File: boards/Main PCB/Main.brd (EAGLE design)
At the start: 101.6 x 76.2 mm, 89 parts, among them CN1 MINIB, CN2 MINIB, IC1 FT232RL, IC2 FT232RL, J1 3_PIN_JST-XH, J2 2_PIN_JST-XH, Q4 BSS138, Q5 BSS138, Q6 BSS138, Q7 BSS138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

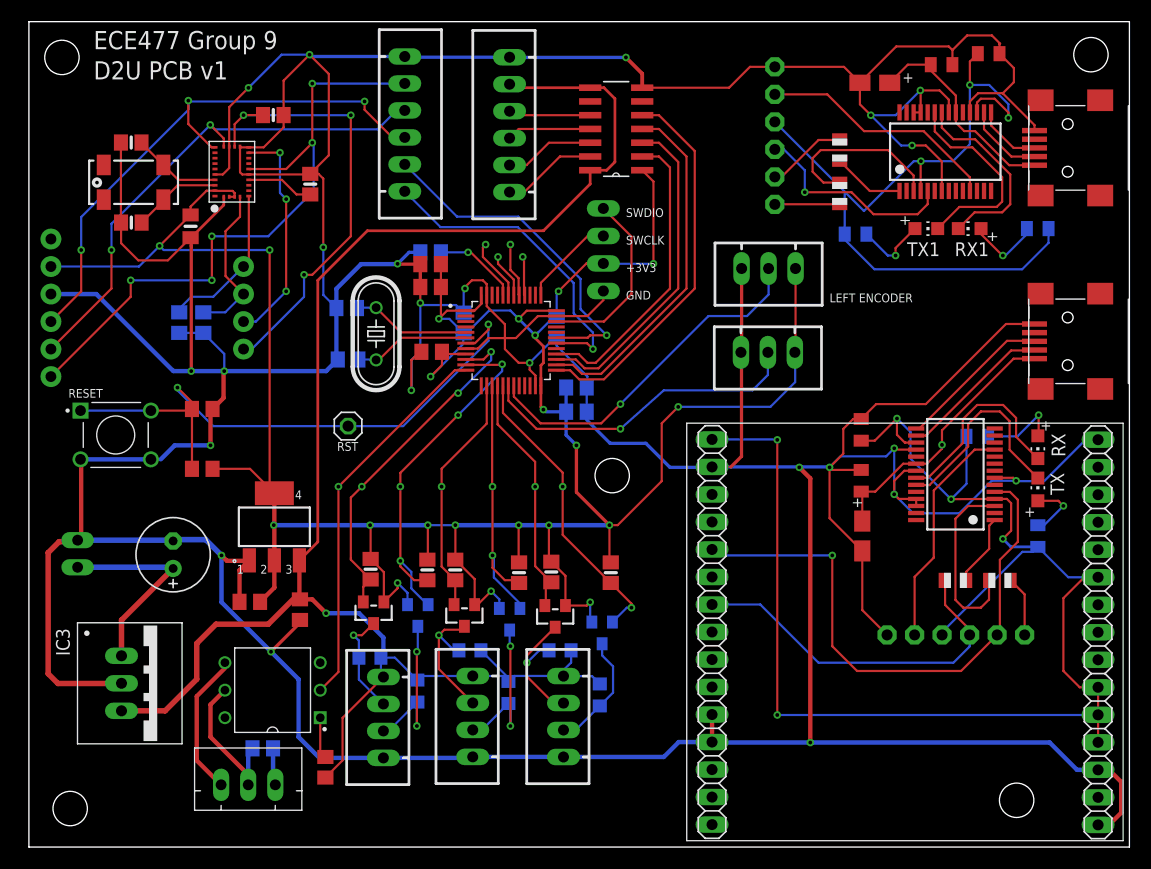
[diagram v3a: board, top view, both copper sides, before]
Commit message: More improvements on trace widths, orientations
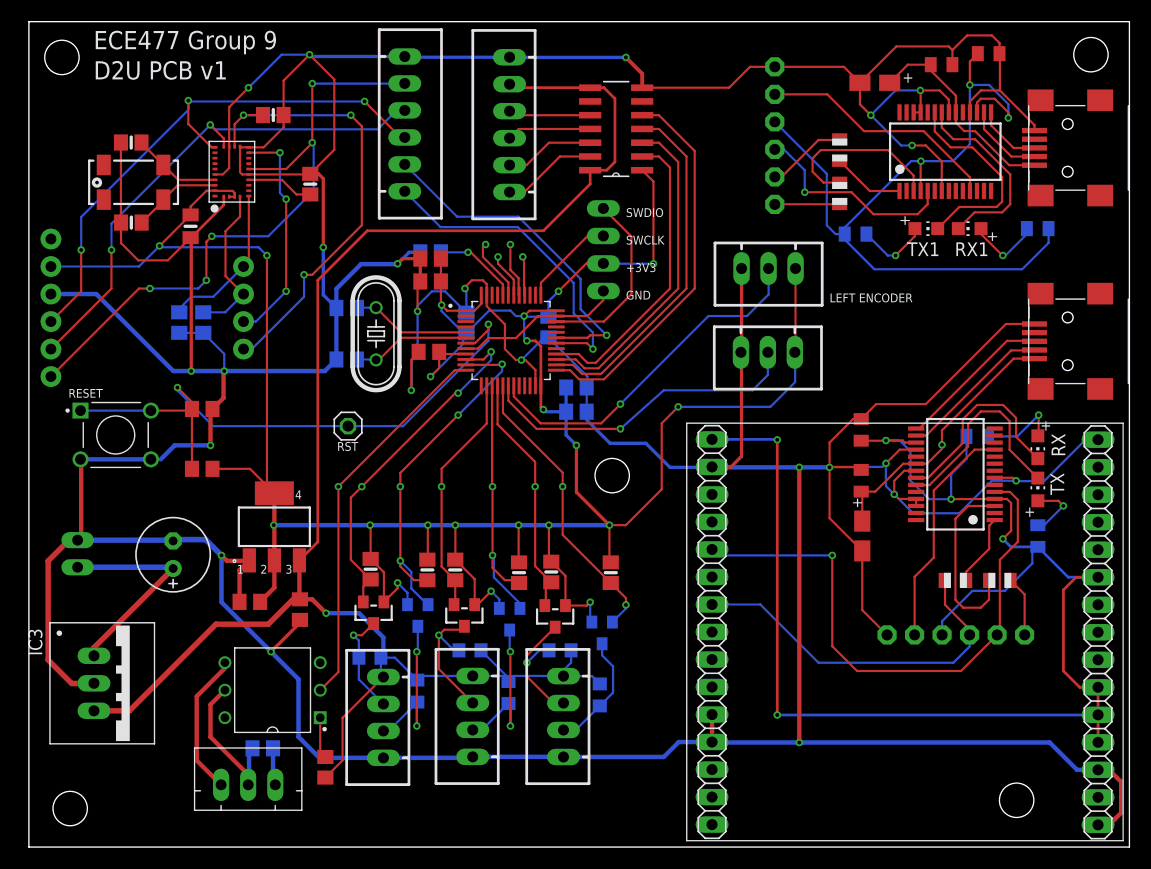
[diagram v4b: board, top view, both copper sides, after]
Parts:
- moved IC3 2.54 mm to (7.28, 15.1)
- moved C24 0.76 mm to (48.0, 48.0)
- moved C20 0.51 mm to (37.1, 54.3)
- moved C25 0.51 mm to (37.1, 52.2)
- moved C22 0.25 mm to (36.9, 45.7)
- moved C21 0.25 mm to (40.4, 48.4)
- moved C15 0.13 mm to (29.3, 45.0)
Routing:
- net GND: track 672.1 -> 668.6 mm
- net NRESET_3V: track 60.0 -> 58.8 mm
- net 12V_IN: track 18.9 -> 20.0 mm
- net +3V3_LIDAR: track 72.6 -> 73.6 mm
- net I2CADDR_3V: track 41.5 -> 42.4 mm
- net US3_ECHO: track 27.7 -> 27.0 mm
- net +3V3_UART_GPS: track 136.3 -> 135.6 mm
- net +5V: track 154.9 -> 155.5 mm

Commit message: More minor trace improvements
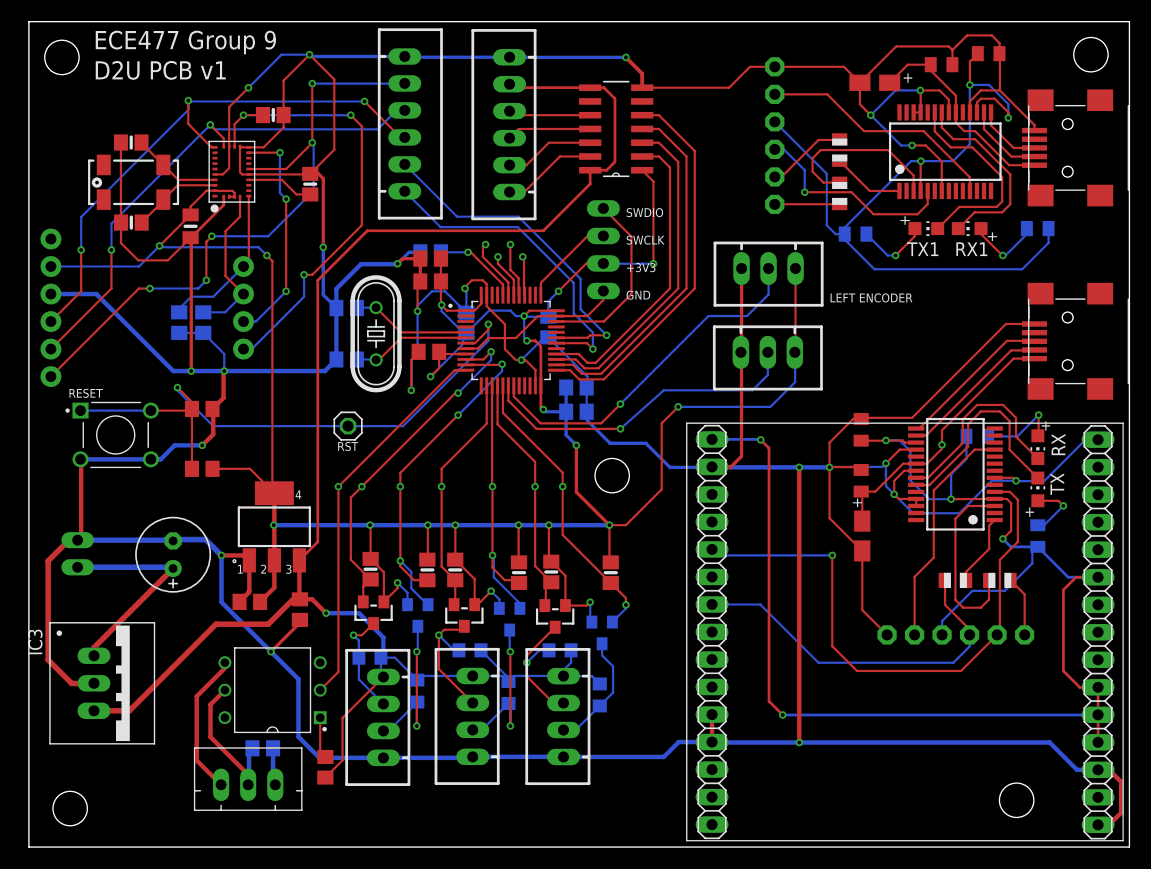
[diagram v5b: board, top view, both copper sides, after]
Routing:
- net +3V3_UART_GPS: track 135.6 -> 134.5 mm
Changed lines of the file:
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@@
 <wire x1="76.936" y1="27.341" x2="76.936" y2="21.876" width="0.2032" layer="1"/>
 <wire x1="76.936" y1="21.876" x2="79.226" y2="19.586" width="0.2032" layer="1"/>
-<wire x1="76.836" y1="39.516" x2="78.214" y2="40.894" width="0.2032" layer="1"/>
-<wire x1="78.214" y1="40.894" x2="82.804" y2="40.894" width="0.2032" layer="1"/>
-<wire x1="82.804" y1="40.894" x2="90.2" y2="48.29" width="0.2032" layer="1"/>
+<wire x1="76.836" y1="39.516" x2="76.944" y2="39.624" width="0.2032" layer="1"/>
+<wire x1="76.944" y1="39.624" x2="81.534" y2="39.624" width="0.2032" layer="1"/>
+<wire x1="81.534" y1="39.624" x2="90.2" y2="48.29" width="0.2032" layer="1"/>
 <wire x1="90.2" y1="48.29" x2="92.836" y2="48.29" width="0.2032" layer="1"/>
 <wire x1="68.862" y1="72.03" x2="75.243" y2="72.03" width="0.2032" layer="1"/>
@@
 <wire x1="4.496" y1="28.332" x2="4.826" y2="28.662" width="0.4064" layer="1"/>
 <wire x1="4.826" y1="35.732" x2="4.764" y2="35.794" width="0.2032" layer="1"/>
-<wire x1="11.264" y1="35.794" x2="12.172" y2="35.794" width="0.2032" layer="16"/>
-<wire x1="13.462" y1="37.084" x2="16.764" y2="37.084" width="0.4064" layer="16"/>
+<wire x1="11.264" y1="35.794" x2="12.172" y2="35.794" width="0.4064" layer="16"/>
+<wire x1="13.462" y1="37.084" x2="16.002" y2="37.084" width="0.4064" layer="16"/>
 <wire x1="12.172" y1="35.794" x2="13.462" y2="37.084" width="0.4064" layer="16"/>
-<via x="16.764" y="37.084" extent="1-16" drill="0.35"/>
-<wire x1="16.764" y1="37.084" x2="16.764" y2="40.256" width="0.4064" layer="1"/>
-<wire x1="16.764" y1="40.256" x2="16.952" y2="40.444" width="0.2032" layer="1"/>
+<via x="16.002" y="37.084" extent="1-16" drill="0.35"/>
+<wire x1="17.018" y1="40.378" x2="17.018" y2="38.1" width="0.4064" layer="1"/>
+<wire x1="16.002" y1="37.084" x2="17.018" y2="38.1" width="0.4064" layer="1"/>
+<wire x1="16.952" y1="40.444" x2="17.018" y2="40.378" width="0.4064" layer="1"/>
 <wire x1="16.952" y1="40.444" x2="17.968" y2="41.46" width="0.4064" layer="1"/>
 <wire x1="27.317" y1="43.942" x2="28.387" y2="45.012" width="0.4064" layer="16"/>
@@
 <wire x1="27.178" y1="50.974" x2="27.178" y2="55.372" width="0.3048" layer="16"/>
 <via x="27.178" y="55.372" extent="1-16" drill="0.35"/>
-<wire x1="19.444" y1="22.638" x2="19.444" y2="25.5646" width="0.4064" layer="1"/>
-<wire x1="19.444" y1="25.5646" x2="20.3077" y2="26.4283" width="0.4064" layer="1"/>
 <via x="34.036" y="53.848" extent="1-16" drill="0.35"/>
 <wire x1="20.3077" y1="26.4283" x2="20.3486" y2="26.4692" width="0.2032" layer="1"/>
@@
 <wire x1="40.974" y1="8.3262" x2="49.342" y2="8.3262" width="0.4064" layer="16"/>
 <wire x1="49.342" y1="8.3262" x2="49.352" y2="8.3162" width="0.2032" layer="16"/>
-<wire x1="18.2757" y1="26.4283" x2="20.3077" y2="26.4283" width="0.4064" layer="1"/>
-<wire x1="17.78" y1="26.924" x2="18.2757" y2="26.4283" width="0.4064" layer="1"/>
 <wire x1="34.698" y1="72.983" x2="26.077" y2="72.983" width="0.3048" layer="16"/>
 <wire x1="26.077" y1="72.983" x2="25.908" y2="73.152" width="0.3048" layer="16"/>
@@
 <wire x1="89.604" y1="73.246" x2="89.64" y2="73.21" width="0.2032" layer="1"/>
 <wire x1="89.64" y1="73.21" x2="89.64" y2="69.85" width="0.2032" layer="1"/>
+<wire x1="17.78" y1="26.924" x2="19.812" y2="26.924" width="0.4064" layer="1"/>
+<wire x1="19.812" y1="26.924" x2="20.3077" y2="26.4283" width="0.4064" layer="1"/>
+<wire x1="20.3486" y1="26.4692" x2="20.3486" y2="23.6173375" width="0.4064" layer="1"/>
+<wire x1="20.3486" y1="23.6173375" x2="20.2876" y2="23.5563375" width="0.4064" layer="1"/>
+<wire x1="20.2876" y1="23.5563375" x2="20.2876" y2="23.4816" width="0.4064" layer="1"/>
+<wire x1="20.2876" y1="23.4816" x2="19.444" y2="22.638" width="0.4064" layer="1"/>
 </signal>
 <signal name="D+_GPS">
@@
 <wire x1="70.739" y1="42.926" x2="70.739" y2="45.6452" width="0.2032" layer="16"/>
 <wire x1="70.739" y1="45.6452" x2="70.7112" y2="45.673" width="0.2032" layer="16"/>
-<wire x1="22.66" y1="32.667" x2="21.971" y2="33.356" width="0.2032" layer="1"/>
-<wire x1="21.971" y1="33.356" x2="21.971" y2="54.61" width="0.2032" layer="1"/>
+<wire x1="22.66" y1="32.667" x2="22.479" y2="32.848" width="0.2032" layer="1"/>
+<wire x1="22.479" y1="54.102" x2="21.971" y2="54.61" width="0.2032" layer="1"/>
+<wire x1="22.479" y1="54.102" x2="22.479" y2="32.848" width="0.2032" layer="1"/>
 <via x="21.971" y="54.61" extent="1-16" drill="0.35"/>
 <wire x1="21.971" y1="54.61" x2="21.209" y2="55.372" width="0.2032" layer="16"/>
@@
 <wire x1="98.703" y1="24.908" x2="96.671" y2="24.908" width="0.254" layer="1"/>
 <wire x1="96.671" y1="24.908" x2="95.504" y2="23.741" width="0.254" layer="1"/>
-<wire x1="63.0668" y1="37.6334" x2="69.0466" y2="37.6334" width="0.254" layer="16"/>
-<wire x1="69.0466" y1="37.6334" x2="69.088" y2="37.592" width="0.2032" layer="16"/>
-<via x="69.088" y="37.592" extent="1-16" drill="0.35"/>
-<wire x1="69.088" y1="37.592" x2="69.088" y2="12.192" width="0.254" layer="1"/>
-<via x="69.088" y="12.192" extent="1-16" drill="0.35"/>
-<wire x1="69.088" y1="12.192" x2="98.687" y2="12.192" width="0.254" layer="16"/>
+<via x="67.564" y="37.592" extent="1-16" drill="0.35"/>
+<wire x1="68.326" y1="36.83" x2="67.564" y2="37.592" width="0.254" layer="1"/>
+<wire x1="68.326" y1="36.83" x2="68.326" y2="13.462" width="0.254" layer="1"/>
+<wire x1="69.596" y1="12.192" x2="68.326" y2="13.462" width="0.254" layer="1"/>
+<via x="69.596" y="12.192" extent="1-16" drill="0.35"/>
+<wire x1="69.596" y1="12.192" x2="98.687" y2="12.192" width="0.254" layer="16"/>
 <wire x1="98.687" y1="12.192" x2="98.703" y2="12.208" width="0.2032" layer="16"/>
 <wire x1="93.144" y1="27.716" x2="95.952" y2="24.908" width="0.254" layer="16"/>
@@
 <wire x1="80.861" y1="37.341" x2="80.668" y2="37.534" width="0.2032" layer="1"/>
 <wire x1="80.668" y1="37.534" x2="79.122" y2="37.534" width="0.2032" layer="1"/>
+<wire x1="67.5226" y1="37.6334" x2="67.564" y2="37.592" width="0.254" layer="16"/>
+<wire x1="63.0668" y1="37.6334" x2="67.5226" y2="37.6334" width="0.254" layer="16"/>
 </signal>
 <signal name="US2_ECHO">

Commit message: Added pullup resistors for SDA and SCL
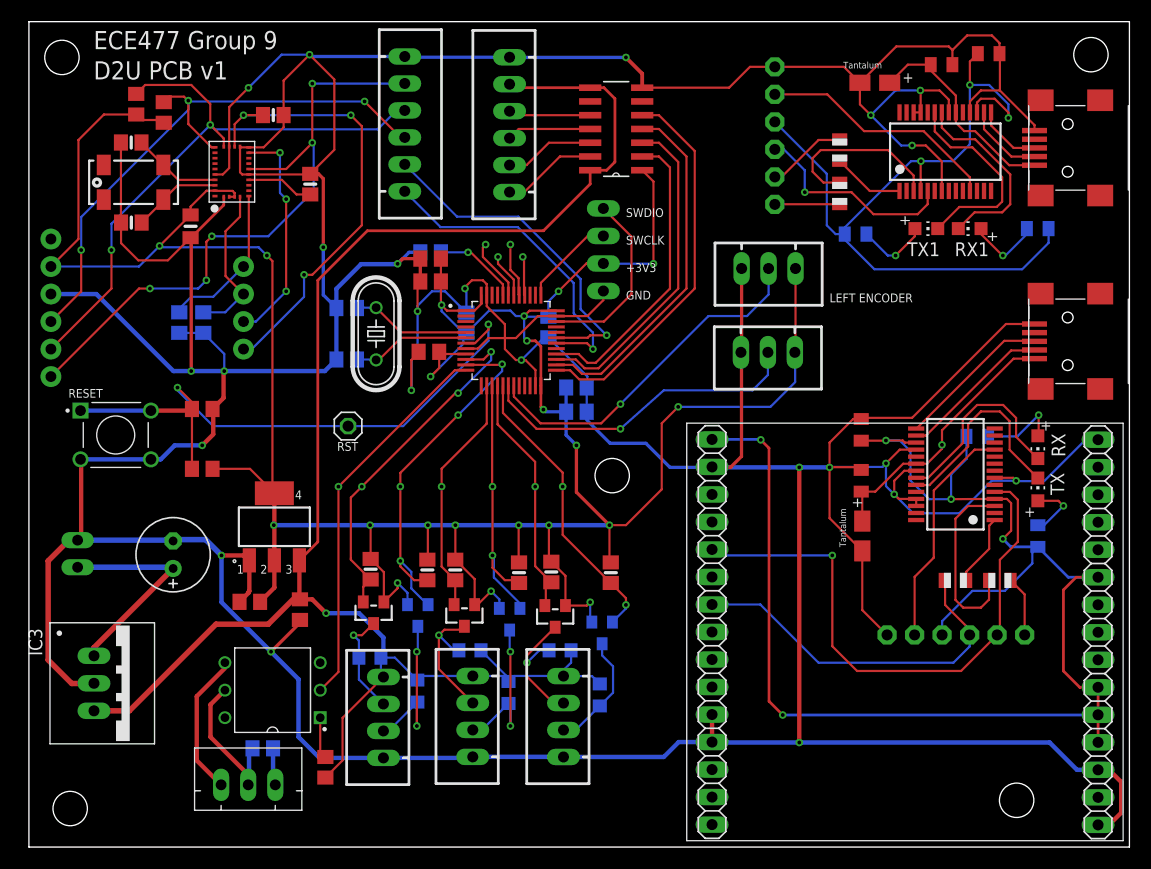
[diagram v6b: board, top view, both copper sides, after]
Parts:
- added R8, R9: 3.3K, resistor:R0805
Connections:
- net +3V3: now also R8.2, R9.2
- net SCL_3V: now also R9.1
- net SDA_3V: now also R8.1
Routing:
- net +3V3: track 269.2 -> 291.1 mm
- net SCL_3V: track 48.2 -> 58.0 mm
- net SDA_3V: track 52.6 -> 55.2 mm
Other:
- board text added: "Tantalum"
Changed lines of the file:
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@@
 <?xml version="1.0" encoding="utf-8"?>
 <!DOCTYPE eagle SYSTEM "eagle.dtd">
-<eagle version="9.2.2">
+<eagle version="9.3.1">
 <drawing>
 <settings>
@@
 <text x="39.37" y="4.318" size="0.8128" layer="26">US2</text>
 <text x="48.006" y="4.318" size="0.8128" layer="26">US3</text>
+<text x="75.184" y="71.882" size="0.6096" layer="25">Tantalum</text>
+<text x="75.438" y="27.686" size="0.6096" layer="25" rot="R90">Tantalum</text>
 </plain>
 <attributes>
@@
 <element name="JP5" library="main_library" package="MICROBUILDER_1X06_ROUND_76" value="" x="2.032" y="49.784" smashed="yes" rot="R270">
 <attribute name="VALUE" x="0.127" y="57.404" size="0.4064" layer="27" ratio="10" rot="R270"/>
+</element>
+<element name="R8" library="resistor" library_urn="urn:adsk.eagle:library:348" package="R0805" package3d_urn="urn:adsk.eagle:package:26059/1" value="3.3K" x="12.446" y="67.818" smashed="yes" rot="R270">
+<attribute name="VALUE" x="13.716" y="67.945" size="0.6096" layer="27" rot="R270"/>
+</element>
+<element name="R9" library="resistor" library_urn="urn:adsk.eagle:library:348" package="R0805" package3d_urn="urn:adsk.eagle:package:26059/1" value="3.3K" x="9.906" y="68.58" smashed="yes" rot="R270">
+<attribute name="VALUE" x="8.128" y="68.707" size="0.6096" layer="27" rot="R270"/>
 </element>
 </elements>
@@
 <contactref element="CN1" pad="D+"/>
 <contactref element="IC1" pad="15"/>
-<wire x1="90.297" y1="46.736" x2="82.202" y2="38.641" width="0.2032" layer="1"/>
-<wire x1="81.911" y1="38.641" x2="82.202" y2="38.641" width="0.2032" layer="1"/>
-<wire x1="90.297" y1="46.736" x2="92.79" y2="46.736" width="0.2032" layer="1"/>
+<wire x1="90.043" y1="46.736" x2="81.948" y2="38.641" width="0.2032" layer="1"/>
+<wire x1="81.911" y1="38.641" x2="81.948" y2="38.641" width="0.2032" layer="1"/>
+<wire x1="92.79" y1="46.736" x2="90.043" y2="46.736" width="0.2032" layer="1"/>
 <wire x1="92.79" y1="46.736" x2="92.836" y2="46.69" width="0.2032" layer="1"/>
 </signal>
@@
 <wire x1="44.45" y1="49.53" x2="44.958" y2="49.022" width="0.2032" layer="16"/>
 <wire x1="44.958" y1="49.022" x2="45.72" y2="49.022" width="0.2032" layer="16"/>
+<wire x1="2.032" y1="53.594" x2="4.572" y2="56.134" width="0.2032" layer="1"/>
+<wire x1="4.572" y1="65.278" x2="4.572" y2="56.134" width="0.2032" layer="1"/>
+<contactref element="R8" pad="2"/>
+<contactref element="R9" pad="2"/>
+<wire x1="9.906" y1="67.63" x2="10.414" y2="67.122" width="0.2032" layer="1"/>
+<wire x1="12.192" y1="67.122" x2="12.446" y2="66.868" width="0.2032" layer="1"/>
+<wire x1="12.192" y1="67.122" x2="10.414" y2="67.122" width="0.2032" layer="1"/>
+<wire x1="9.906" y1="67.63" x2="6.924" y2="67.63" width="0.2032" layer="1"/>
+<wire x1="6.924" y1="67.63" x2="4.572" y2="65.278" width="0.2032" layer="1"/>
 </signal>
 <signal name="N$6">
@@
 <wire x1="4.826" y1="55.118" x2="4.826" y2="51.308" width="0.2032" layer="1"/>
 <wire x1="4.826" y1="51.308" x2="2.032" y2="48.514" width="0.2032" layer="1"/>
+<contactref element="R8" pad="1"/>
+<wire x1="14.716" y1="68.91" x2="14.686" y2="68.91" width="0.2032" layer="1"/>
+<wire x1="14.686" y1="68.91" x2="14.32" y2="69.276" width="0.2032" layer="1"/>
+<wire x1="14.32" y1="69.276" x2="12.954" y2="69.276" width="0.2032" layer="1"/>
+<wire x1="12.954" y1="69.276" x2="12.446" y2="68.768" width="0.2032" layer="1"/>
 </signal>
 <signal name="SCL_3V">
@@
 <wire x1="7.62" y1="55.118" x2="7.62" y2="57.544" width="0.2032" layer="16"/>
 <wire x1="7.62" y1="57.544" x2="16.743" y2="66.667" width="0.2032" layer="16"/>
+<contactref element="R9" pad="1"/>
+<wire x1="16.743" y1="66.667" x2="16.743" y2="68.601" width="0.2032" layer="1"/>
+<wire x1="16.743" y1="68.601" x2="14.986" y2="70.358" width="0.2032" layer="1"/>
+<wire x1="14.986" y1="70.358" x2="10.734" y2="70.358" width="0.2032" layer="1"/>
+<wire x1="10.734" y1="70.358" x2="9.906" y2="69.53" width="0.2032" layer="1"/>
 </signal>
 <signal name="N$1">
@@
 <contactref element="RESET" pad="2"/>
 <contactref element="RESET" pad="1"/>
-<wire x1="11.264" y1="40.294" x2="4.764" y2="40.294" width="0.2032" layer="16"/>
+<wire x1="11.264" y1="40.294" x2="4.764" y2="40.294" width="0.4064" layer="16"/>
 <wire x1="15.052" y1="40.444" x2="15.052" y2="34.918" width="0.2032" layer="1"/>
 <via x="13.716" y="42.418" extent="1-16" drill="0.35"/>
@@
 <wire x1="42.418" y1="47.752" x2="42.418" y2="48.26" width="0.2032" layer="1"/>
 <wire x1="41.184" y1="46.518" x2="42.418" y2="47.752" width="0.2032" layer="1"/>
-<wire x1="11.264" y1="40.294" x2="14.902" y2="40.294" width="0.2032" layer="1"/>
+<wire x1="11.264" y1="40.294" x2="14.902" y2="40.294" width="0.4064" layer="1"/>
 <wire x1="14.902" y1="40.294" x2="15.052" y2="40.444" width="0.2032" layer="1"/>
 <contactref element="JP3" pad="1"/>
